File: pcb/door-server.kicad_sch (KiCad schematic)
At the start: 18 parts, among them CN1 KF2EDGR-3.5-2P, CN10 KF2EDGR-3.5-2P, CN14 KF2EDGR-3.5-2P, CN18 KF2EDGR-3.5-2P, CN2 KF2EDGR-3.5-2P, CN3 KF2EDGR-3.5-2P, CN4 KF2EDGR-3.5-4P, CN5 KF2EDGR-3.5-7P, CN6 KF2EDGR-3.5-4P, CN8 KF2EDGR-3.5-2P, J1 KF2EDGR-3.5-4P, J2 KF2EDGR-3.5-4P, J3 KF2EDGR-3.5-4P, J4 KF2EDGR-3.5-4P, J5 KF2EDGR-3.5-4P, J6 6P2C, U9 Raspberry_Pi_2_3

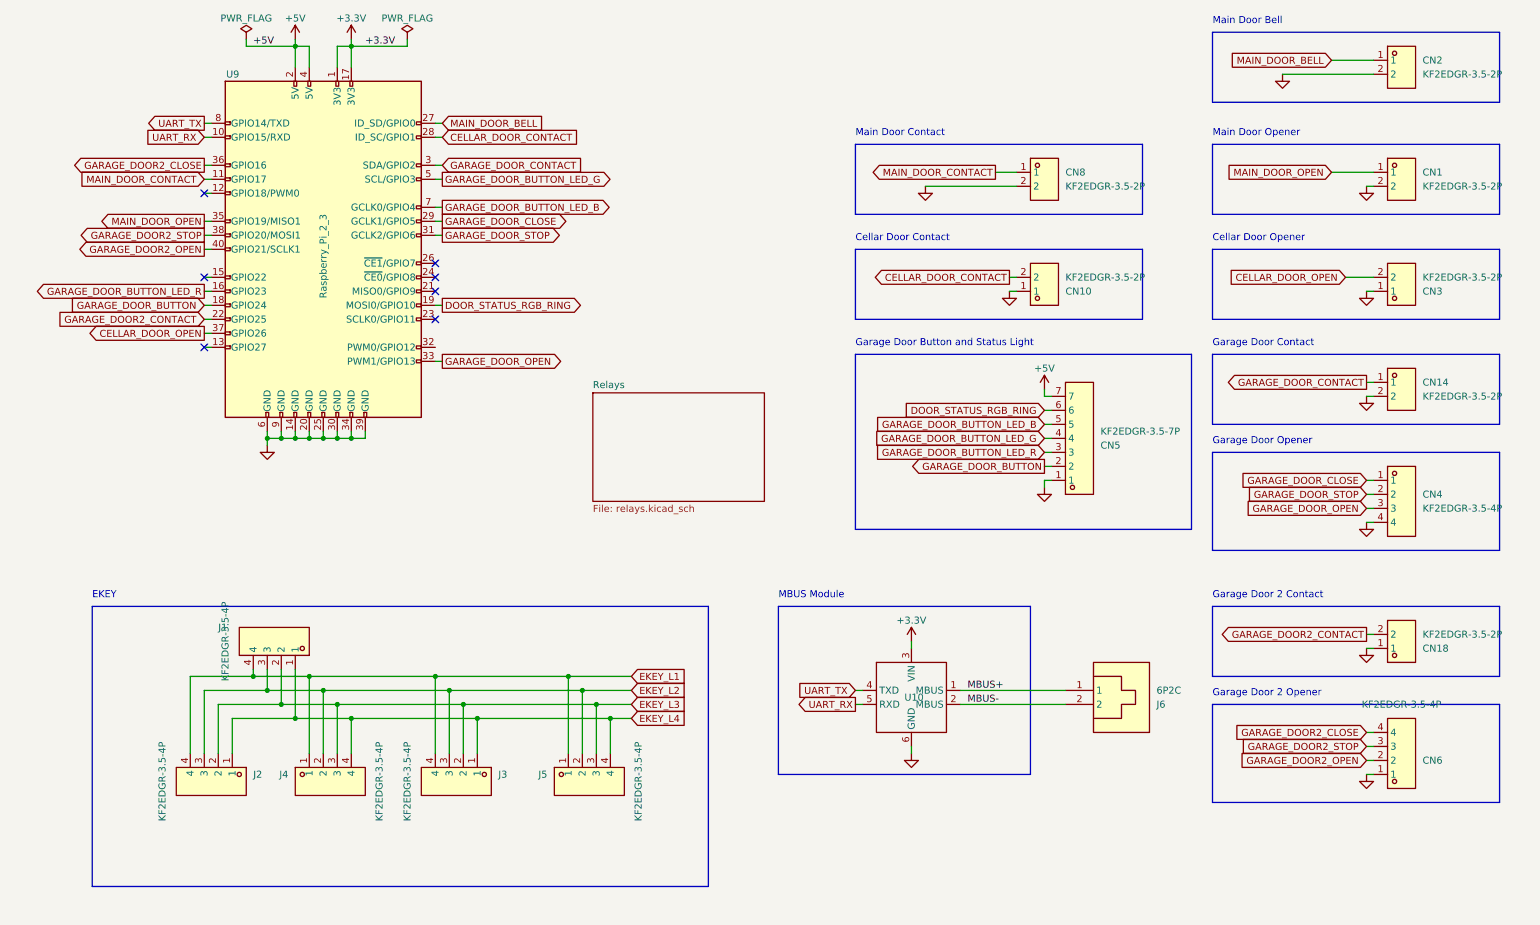
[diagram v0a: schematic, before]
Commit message: Improve PCB layout and connectors.
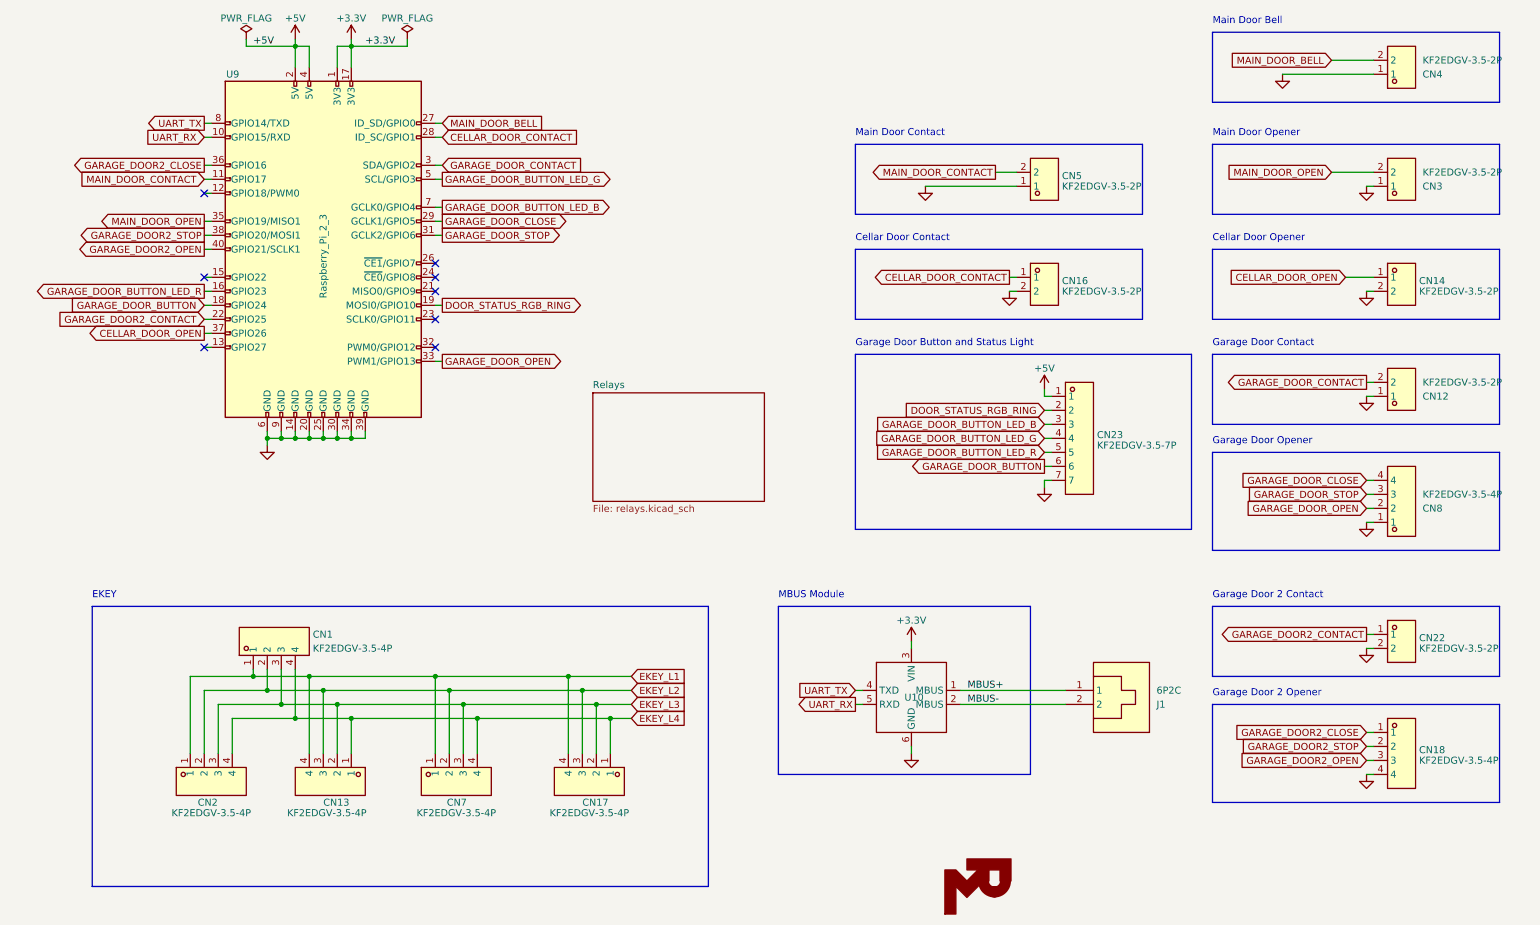
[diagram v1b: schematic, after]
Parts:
- CN1: renamed from J1; value KF2EDGR-3.5-4P -> KF2EDGV-3.5-4P; footprint easyeda2kicad:CONN-TH_4P-P3.50_KF2EDGR-3.5-4P -> easyeda2kicad:CONN-TH_4P-P3.50_KF2EDGV-3.5-4P; symbol easyeda2kicad:KF2EDGR-3.5-4P -> easyeda2kicad:KF2EDGV-3.5-4P; LCSC Part C441173 -> C441323
- CN12: renamed from CN14; value KF2EDGR-3.5-2P -> KF2EDGV-3.5-2P; footprint easyeda2kicad:CONN-TH_2P-P3.50_KF2EDGR-3.5-2P -> easyeda2kicad:CONN-TH_2P_P3.50_KF2EDGV-3.5-2P; symbol easyeda2kicad:KF2EDGR-3.5-2P -> easyeda2kicad:KF2EDGV-3.5-2P; LCSC Part C441171 -> C441321
- CN13: renamed from J4; value KF2EDGR-3.5-4P -> KF2EDGV-3.5-4P; footprint easyeda2kicad:CONN-TH_4P-P3.50_KF2EDGR-3.5-4P -> easyeda2kicad:CONN-TH_4P-P3.50_KF2EDGV-3.5-4P; symbol easyeda2kicad:KF2EDGR-3.5-4P -> easyeda2kicad:KF2EDGV-3.5-4P; LCSC Part C441173 -> C441323
- CN14: renamed from CN3; value KF2EDGR-3.5-2P -> KF2EDGV-3.5-2P; footprint easyeda2kicad:CONN-TH_2P-P3.50_KF2EDGR-3.5-2P -> easyeda2kicad:CONN-TH_2P_P3.50_KF2EDGV-3.5-2P; symbol easyeda2kicad:KF2EDGR-3.5-2P -> easyeda2kicad:KF2EDGV-3.5-2P; LCSC Part C441171 -> C441321
- CN16: renamed from CN10; value KF2EDGR-3.5-2P -> KF2EDGV-3.5-2P; footprint easyeda2kicad:CONN-TH_2P-P3.50_KF2EDGR-3.5-2P -> easyeda2kicad:CONN-TH_2P_P3.50_KF2EDGV-3.5-2P; symbol easyeda2kicad:KF2EDGR-3.5-2P -> easyeda2kicad:KF2EDGV-3.5-2P; LCSC Part C441171 -> C441321
- CN17: renamed from J5; value KF2EDGR-3.5-4P -> KF2EDGV-3.5-4P; footprint easyeda2kicad:CONN-TH_4P-P3.50_KF2EDGR-3.5-4P -> easyeda2kicad:CONN-TH_4P-P3.50_KF2EDGV-3.5-4P; symbol easyeda2kicad:KF2EDGR-3.5-4P -> easyeda2kicad:KF2EDGV-3.5-4P; LCSC Part C441173 -> C441323
- CN18: renamed from CN6; value KF2EDGR-3.5-4P -> KF2EDGV-3.5-4P; footprint easyeda2kicad:CONN-TH_4P-P3.50_KF2EDGR-3.5-4P -> easyeda2kicad:CONN-TH_4P-P3.50_KF2EDGV-3.5-4P; symbol easyeda2kicad:KF2EDGR-3.5-4P -> easyeda2kicad:KF2EDGV-3.5-4P; LCSC Part C441173 -> C441323
- CN2: renamed from J2; value KF2EDGR-3.5-4P -> KF2EDGV-3.5-4P; footprint easyeda2kicad:CONN-TH_4P-P3.50_KF2EDGR-3.5-4P -> easyeda2kicad:CONN-TH_4P-P3.50_KF2EDGV-3.5-4P; symbol easyeda2kicad:KF2EDGR-3.5-4P -> easyeda2kicad:KF2EDGV-3.5-4P; LCSC Part C441173 -> C441323
- CN22: renamed from CN18; value KF2EDGR-3.5-2P -> KF2EDGV-3.5-2P; footprint easyeda2kicad:CONN-TH_2P-P3.50_KF2EDGR-3.5-2P -> easyeda2kicad:CONN-TH_2P_P3.50_KF2EDGV-3.5-2P; symbol easyeda2kicad:KF2EDGR-3.5-2P -> easyeda2kicad:KF2EDGV-3.5-2P; LCSC Part C441171 -> C441321
- CN23: renamed from CN5; value KF2EDGR-3.5-7P -> KF2EDGV-3.5-7P; footprint easyeda2kicad:CONN-TH_7P-P3.50_KF2EDGR-3.5-7P -> easyeda2kicad:CONN-TH_7P-P3.50_KF2EDGV-3.5-7P; symbol easyeda2kicad:KF2EDGR-3.5-7P -> easyeda2kicad:KF2EDGV-3.5-7P; LCSC Part C441176 -> C441326
- CN3: renamed from CN1; value KF2EDGR-3.5-2P -> KF2EDGV-3.5-2P; footprint easyeda2kicad:CONN-TH_2P-P3.50_KF2EDGR-3.5-2P -> easyeda2kicad:CONN-TH_2P_P3.50_KF2EDGV-3.5-2P; symbol easyeda2kicad:KF2EDGR-3.5-2P -> easyeda2kicad:KF2EDGV-3.5-2P; LCSC Part C441171 -> C441321
- CN4: renamed from CN2; value KF2EDGR-3.5-2P -> KF2EDGV-3.5-2P; footprint easyeda2kicad:CONN-TH_2P-P3.50_KF2EDGR-3.5-2P -> easyeda2kicad:CONN-TH_2P_P3.50_KF2EDGV-3.5-2P; symbol easyeda2kicad:KF2EDGR-3.5-2P -> easyeda2kicad:KF2EDGV-3.5-2P; LCSC Part C441171 -> C441321
- CN5: renamed from CN8; value KF2EDGR-3.5-2P -> KF2EDGV-3.5-2P; footprint easyeda2kicad:CONN-TH_2P-P3.50_KF2EDGR-3.5-2P -> easyeda2kicad:CONN-TH_2P_P3.50_KF2EDGV-3.5-2P; symbol easyeda2kicad:KF2EDGR-3.5-2P -> easyeda2kicad:KF2EDGV-3.5-2P; LCSC Part C441171 -> C441321
- CN7: renamed from J3; value KF2EDGR-3.5-4P -> KF2EDGV-3.5-4P; footprint easyeda2kicad:CONN-TH_4P-P3.50_KF2EDGR-3.5-4P -> easyeda2kicad:CONN-TH_4P-P3.50_KF2EDGV-3.5-4P; symbol easyeda2kicad:KF2EDGR-3.5-4P -> easyeda2kicad:KF2EDGV-3.5-4P; LCSC Part C441173 -> C441323
- CN8: renamed from CN4; value KF2EDGR-3.5-4P -> KF2EDGV-3.5-4P; footprint easyeda2kicad:CONN-TH_4P-P3.50_KF2EDGR-3.5-4P -> easyeda2kicad:CONN-TH_4P-P3.50_KF2EDGV-3.5-4P; symbol easyeda2kicad:KF2EDGR-3.5-4P -> easyeda2kicad:KF2EDGV-3.5-4P; LCSC Part C441173 -> C441323
- J1: renamed from J6; footprint easyeda2kicad:RJ11-TH_55A-1X1-6P2C-E-13H -> easyeda2kicad:RJ11-TH_55A-1X1-6P2C-E-13H_HC-WK62-MIH12-G; symbol easyeda2kicad:PCB-6P2C-90_C189745 -> easyeda2kicad:HC-WK62-MIH12-G; LCSC Part C189745 -> C7501840
- U9: footprint logo:PinSocket_2x20_P2.54mm_Vertical_RaspberryPi -> MR-Logo:PinSocket_2x20_P2.54mm_Vertical_RaspberryPi; LCSC Part C50982 -> C2685116
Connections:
- net +5V: now also CN23.1; no longer CN23.7
- net CELLAR_DOOR_CONTACT: now also CN16.1; no longer CN16.2
- net CELLAR_DOOR_OPEN: now also CN14.1; no longer CN14.2
- net DOOR_STATUS_RGB_RING: now also CN23.2; no longer CN23.6
- net EKEY_L1: now also CN1.1, CN13.4, CN17.4, CN2.1, CN7.1; no longer CN1.4, CN13.1, CN17.1, CN2.4, CN7.4
- net EKEY_L2: now also CN1.2, CN13.3, CN17.3, CN2.2, CN7.2; no longer CN1.3, CN13.2, CN17.2, CN2.3, CN7.3
- net EKEY_L3: now also CN1.3, CN13.2, CN17.2, CN2.3, CN7.3; no longer CN1.2, CN13.3, CN17.3, CN2.2, CN7.2
- net EKEY_L4: now also CN1.4, CN13.1, CN17.1, CN2.4, CN7.4; no longer CN1.1, CN13.4, CN17.4, CN2.1, CN7.1
- net GARAGE_DOOR2_CLOSE: now also CN18.1; no longer CN18.4
- net GARAGE_DOOR2_CONTACT: now also CN22.1; no longer CN22.2
- net GARAGE_DOOR2_OPEN: now also CN18.3; no longer CN18.2
- net GARAGE_DOOR2_STOP: now also CN18.2; no longer CN18.3
- net GARAGE_DOOR_BUTTON: now also CN23.6; no longer CN23.2
- net GARAGE_DOOR_BUTTON_LED_B: now also CN23.3; no longer CN23.5
- net GARAGE_DOOR_BUTTON_LED_R: now also CN23.5; no longer CN23.3
- net GARAGE_DOOR_CLOSE: now also CN8.4; no longer CN8.1
- net GARAGE_DOOR_CONTACT: now also CN12.2; no longer CN12.1
- net GARAGE_DOOR_OPEN: now also CN8.2; no longer CN8.3
- net GARAGE_DOOR_STOP: now also CN8.3; no longer CN8.2
- net GND: now also CN12.1, CN14.2, CN16.2, CN18.4, CN22.2, CN23.7, CN3.1, CN4.1, CN5.1, CN8.1; no longer CN12.2, CN14.1, CN16.1, CN18.1, CN22.1, CN23.1, CN3.2, CN4.2, CN5.2, CN8.4
- net MAIN_DOOR_BELL: now also CN4.2; no longer CN4.1
- net MAIN_DOOR_CONTACT: now also CN5.2; no longer CN5.1
- net MAIN_DOOR_OPEN: now also CN3.2; no longer CN3.1
- no-connect marks 7 -> 8
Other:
- moved on the sheet: CN1, CN13, CN17, CN2, CN7

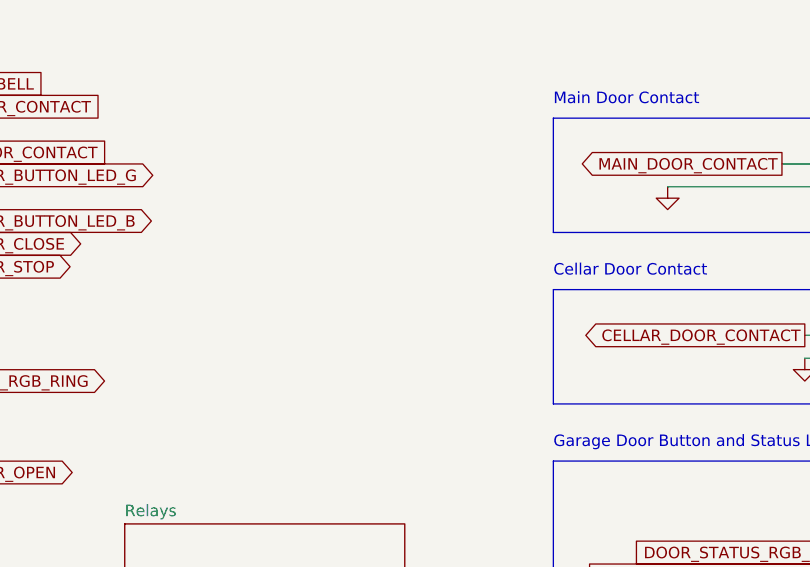
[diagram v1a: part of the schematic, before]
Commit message: Add power supply to PCB.
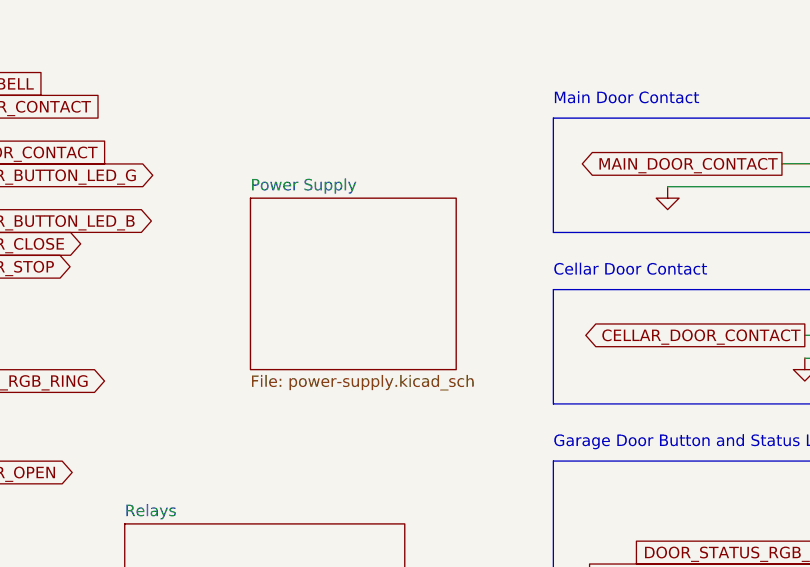
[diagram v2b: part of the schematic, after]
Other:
- added sheet Power Supply (power-supply.kicad_sch)
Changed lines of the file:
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@@
+    )
+  )
+  (sheet (at 130.175 48.26) (size 22.86 19.05) (fields_autoplaced)
+    (stroke (width 0.1524) (type solid))
+    (fill (color 0 0 0 0.0000))
+    (property "Sheetname" "Power Supply" (at 130.175 47.5484 0)
+      (effects (font (size 1.27 1.27)) (justify left bottom))
+    )
+    (property "Sheetfile" "power-supply.kicad_sch" (at 130.175 67.8946 0)
+      (effects (font (size 1.27 1.27)) (justify left top))
+    )
+    (instances
+      (project "door-server"
+        (path "/3837392b-f24c-487e-8a15-3e756935fe56" (page "3"))
+      )
     )
   )
